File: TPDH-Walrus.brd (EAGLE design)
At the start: 16 x 39.9 mm, 45 parts, among them Q2 DMG3404, U1 MS5803-14BA, U2 SN65HVD33RHL, U4 MCP3421A3, U5 TPS79733, U6 MAX6070AAUT18, U7 TXS0102DQM

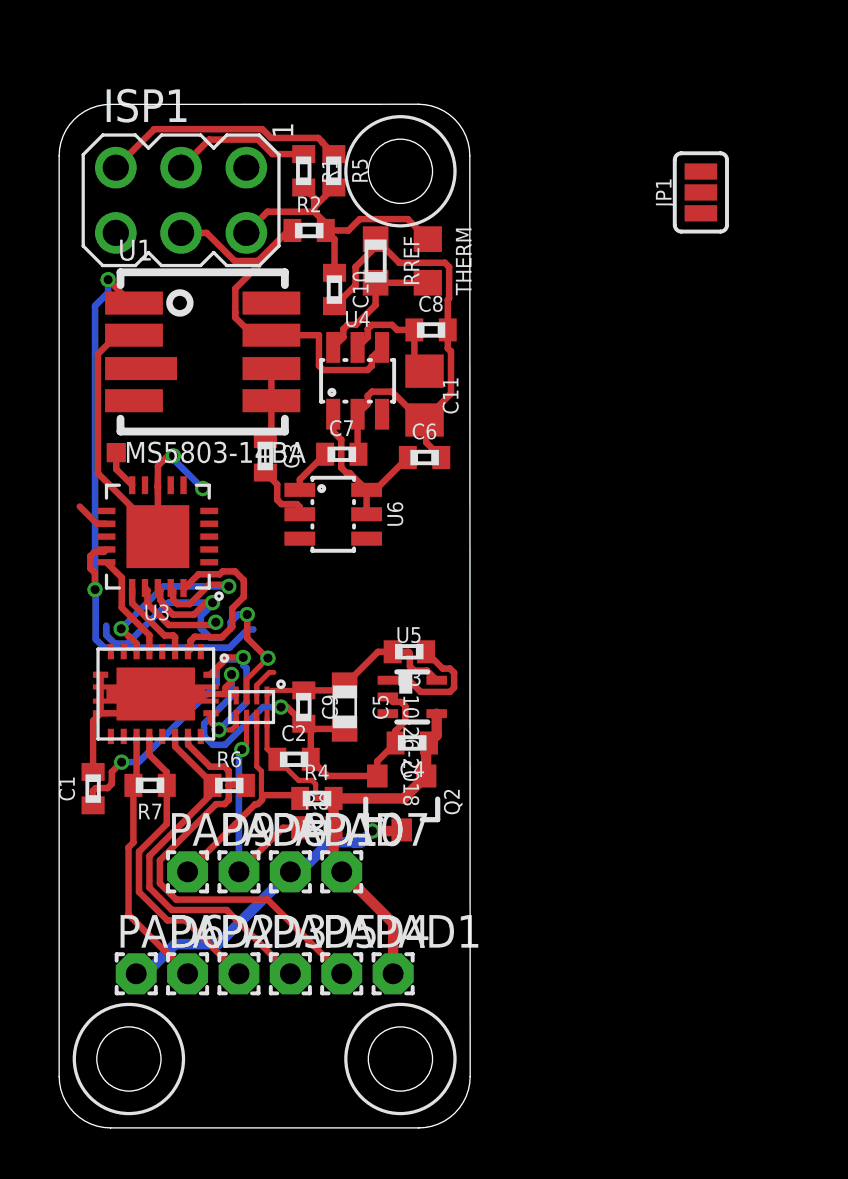
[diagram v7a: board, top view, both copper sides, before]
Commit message: mostly routed
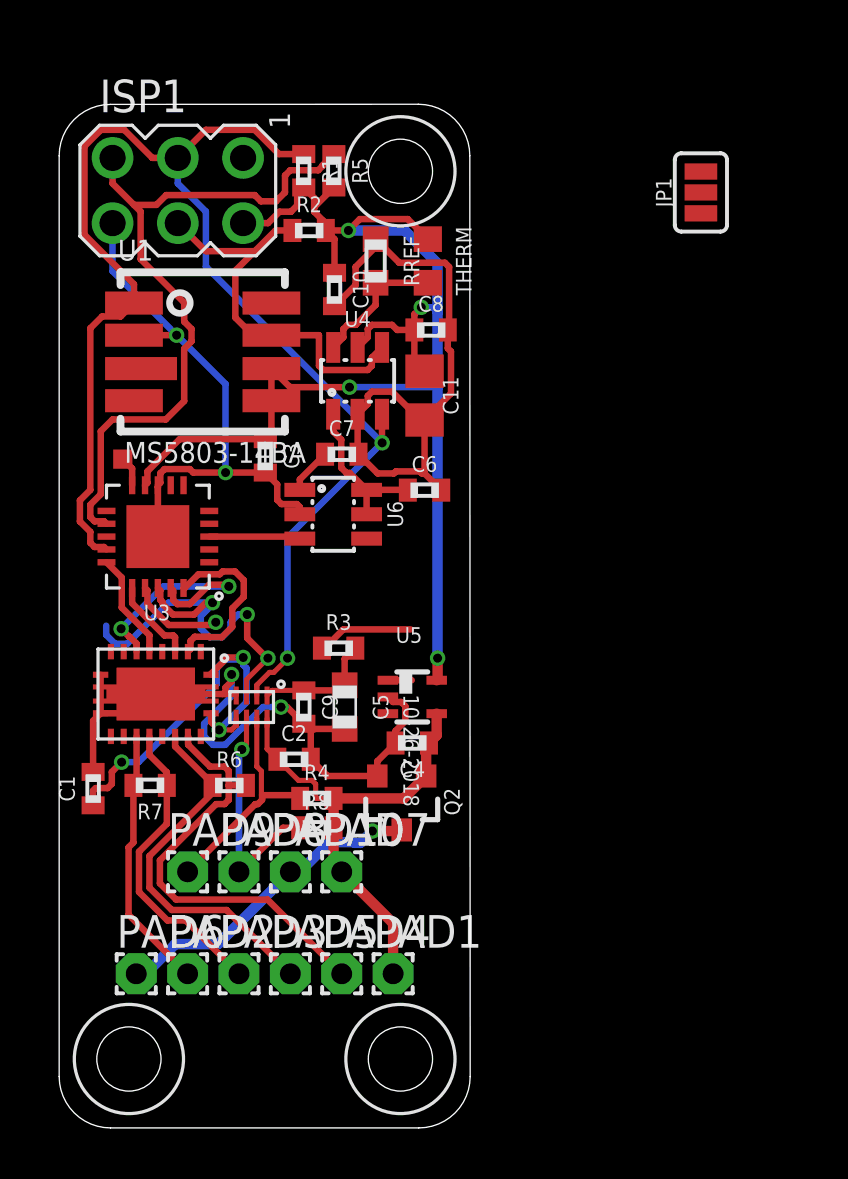
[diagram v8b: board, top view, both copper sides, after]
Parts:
- moved R3 2.76 mm to (10.9, 18.7), turned to 0 degrees
- moved C6 1.27 mm to (14.2, 24.8)
- moved ISP1 0.40 mm to (4.62, 36.5)
- moved U$12 0.36 mm to (2.48, 26.0)
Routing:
- net +3V3: track 45.1 -> 76.4 mm, vias 3 -> 7
- net SCL: track 31.0 -> 56.0 mm
- net /RESET: track 10.8 -> 28.0 mm
- net GND: track 65.7 -> 75.4 mm
- net REF_EN: track 0.00 -> 3.56 mm
- net SPI-I2C-SWITCH: track 1.13 -> 0.00 mm
- net VREF: track 6.63 -> 6.12 mm
